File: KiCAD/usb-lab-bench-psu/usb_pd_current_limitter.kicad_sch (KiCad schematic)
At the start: 12 parts, among them J24 Conn_02x03_Top_Bottom, Q3 PMOS, U15 DAC53401, U16 MCP602

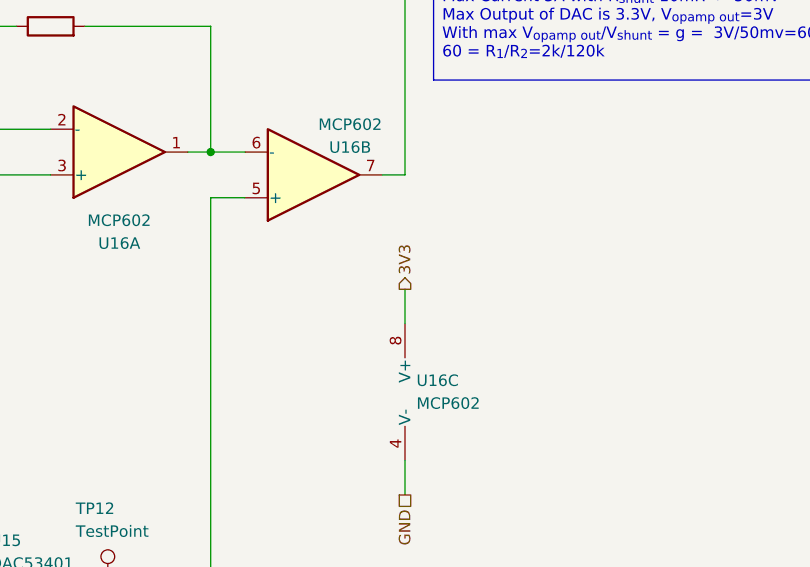
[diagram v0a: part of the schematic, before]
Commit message: Fixed label directions
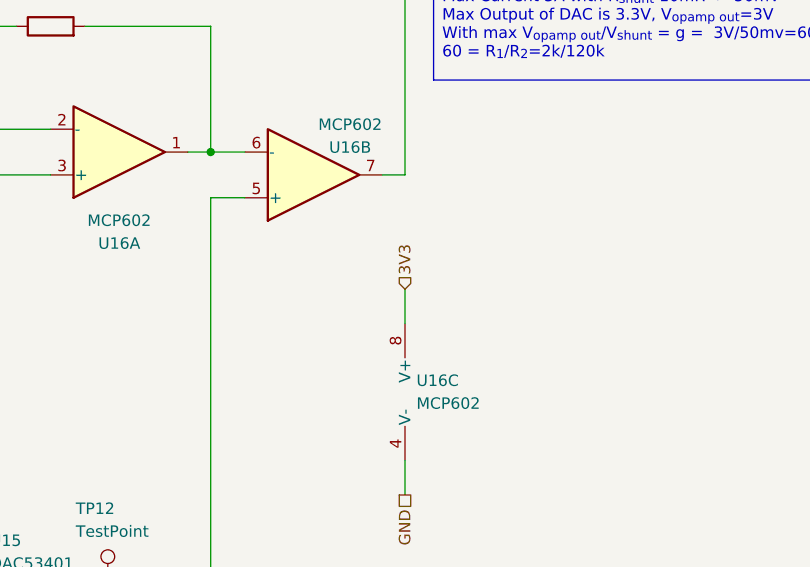
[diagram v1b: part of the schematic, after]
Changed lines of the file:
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@@
 	)
 	(hierarchical_label "3V3"
-		(shape output)
+		(shape input)
 		(at 154.94 85.09 90)
 		(effects

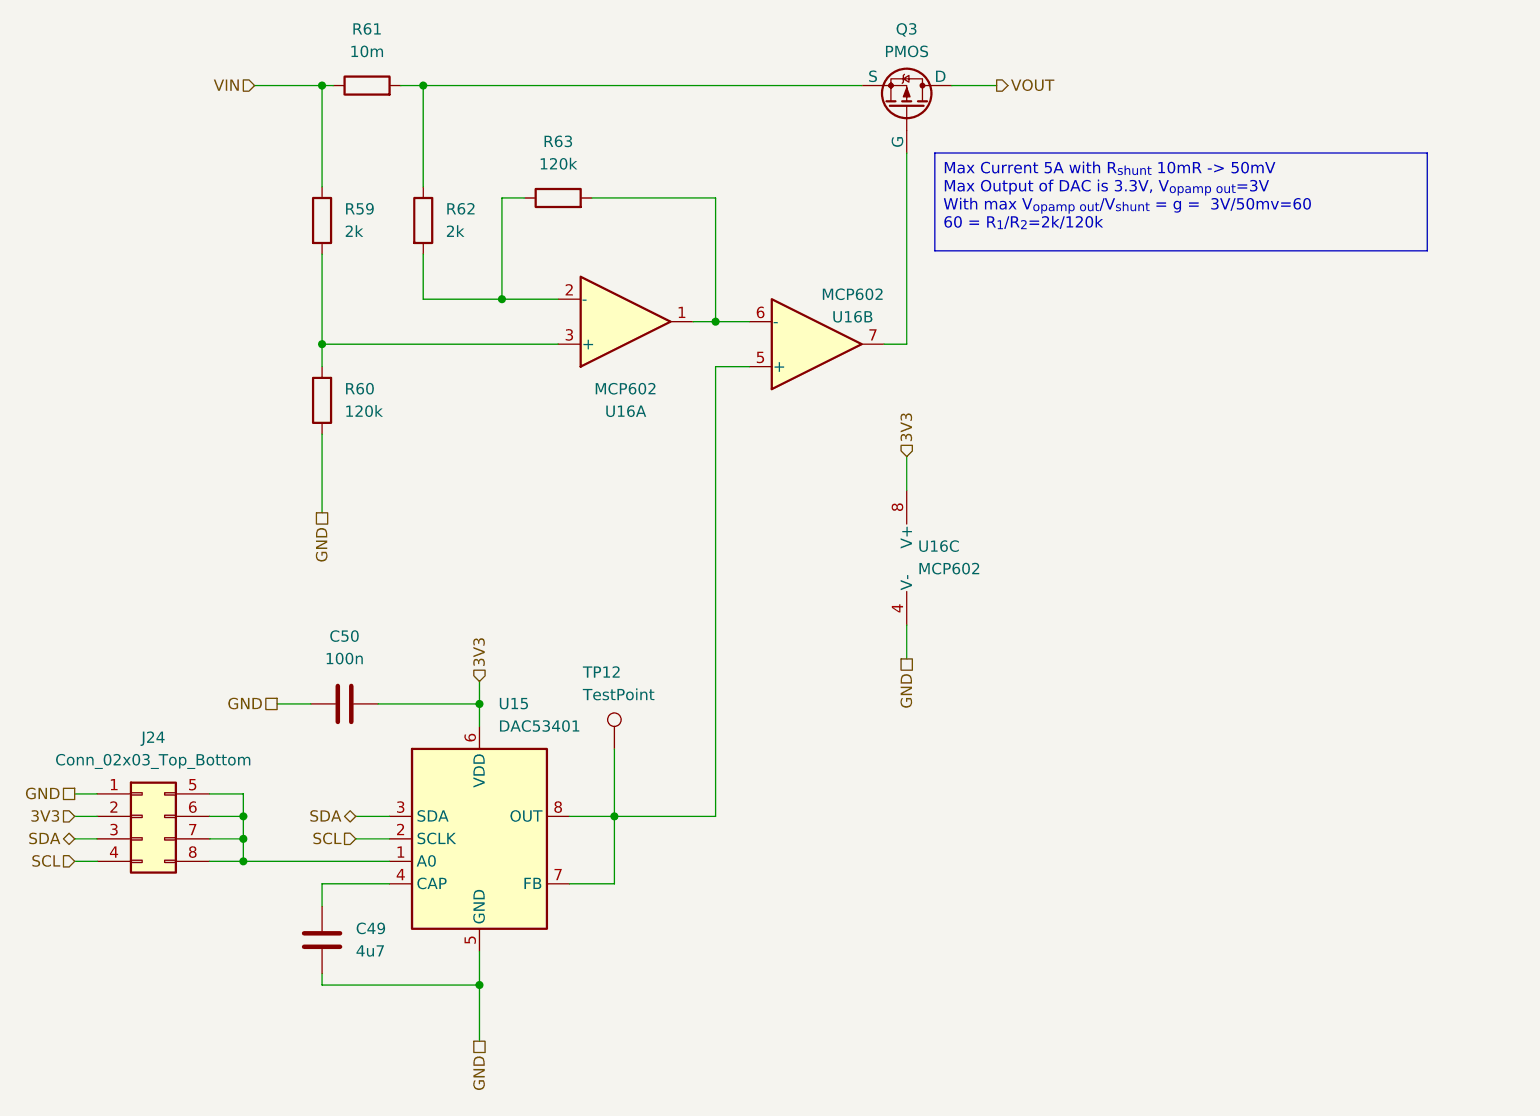
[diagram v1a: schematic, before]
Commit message: tweaked design of current limiter, added GPIO expander to USB-PD circuit
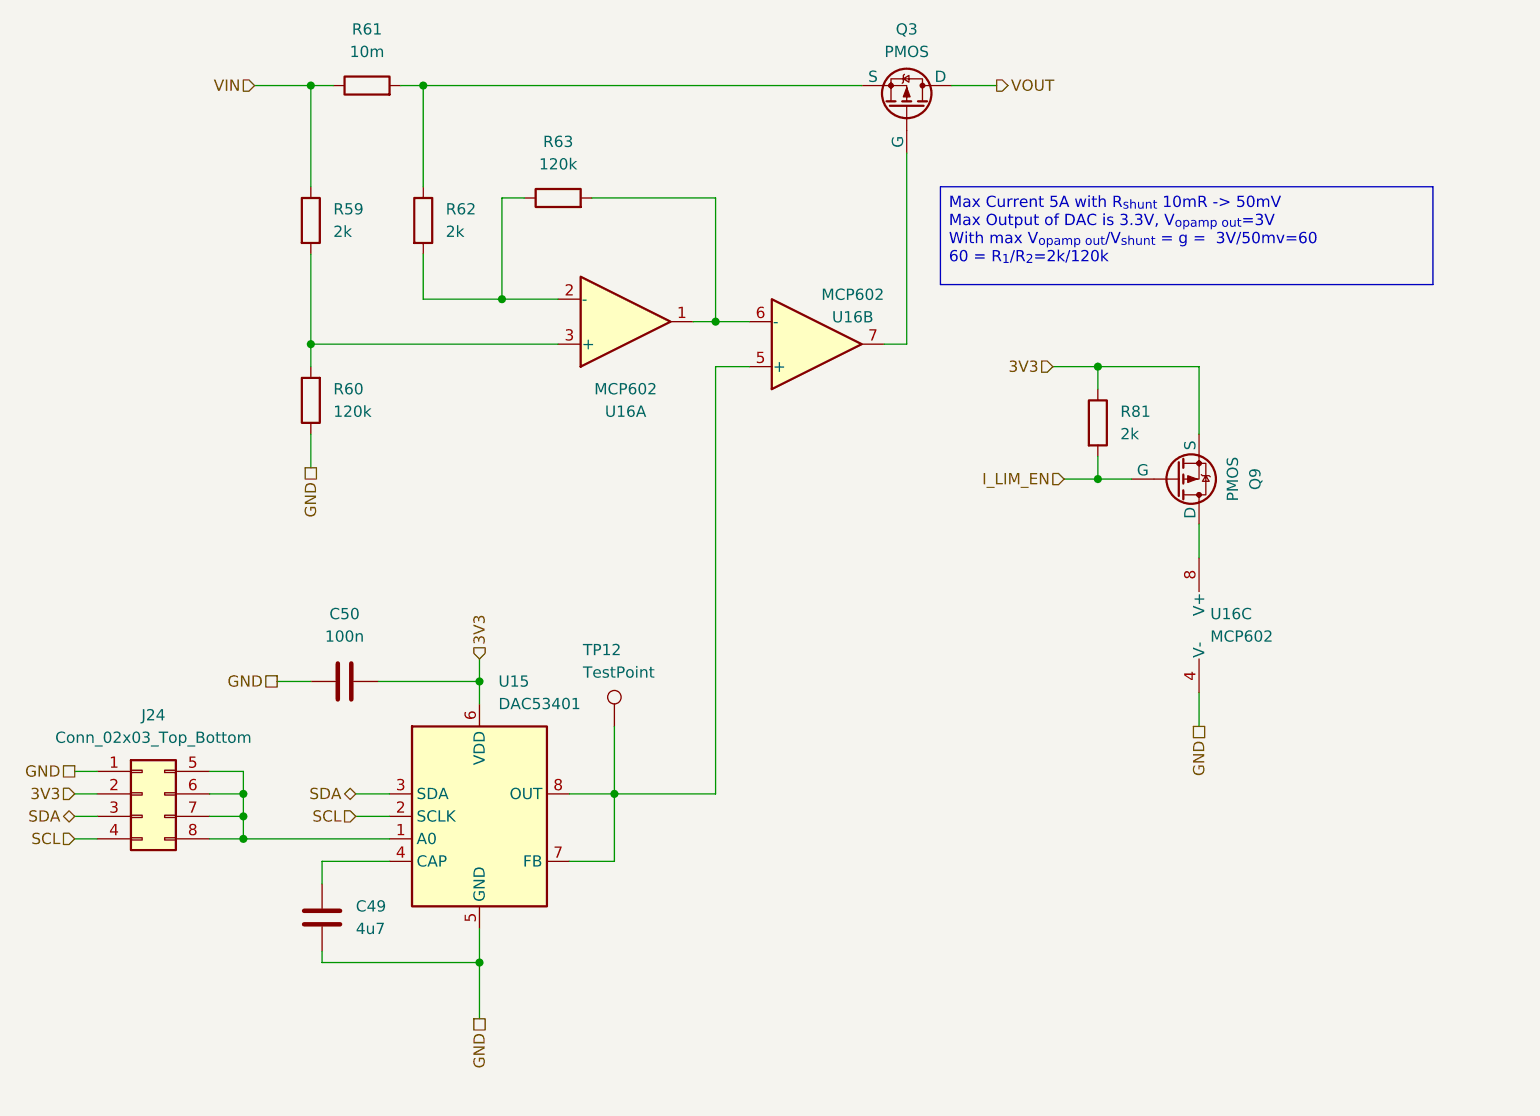
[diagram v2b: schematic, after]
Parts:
- added Q9: PMOS, symbol Simulation_SPICE:PMOS
- added R81: 2k, symbol Device:R
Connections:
- net 3V3: now also Q9.3 (S), R81.1; no longer U16.8 (V+)
- new net: Q9.1 (D), U16.8 (V+)
- new net I_LIM_EN: Q9.2 (G), R81.2
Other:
- moved on the sheet: C49, C50, J24, R59, R60, TP12, U15, U16C
